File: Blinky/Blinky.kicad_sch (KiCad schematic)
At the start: 69 parts, among them J1 Conn_01x06_Socket, J2 Conn_01x06_Socket, J3 Battery Connector, J4 Charging Notches, Q1 IRLML6244, Q2 IRLML6244, Q3 IRLML6244, Q4 IRLML6244, Q5 IRLML6244, Q6 IRLML6244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

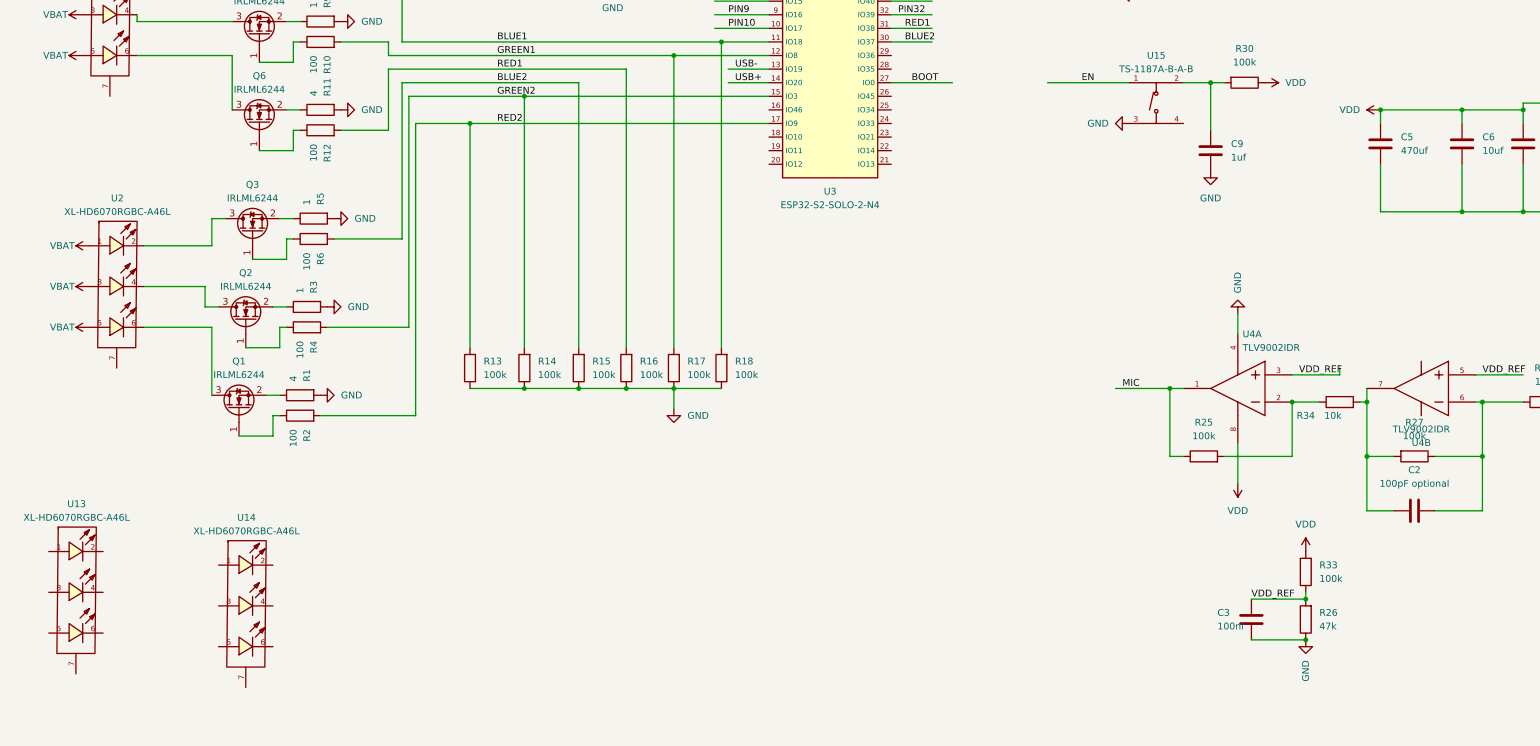
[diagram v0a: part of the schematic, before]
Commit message: reordered and fixed stuff
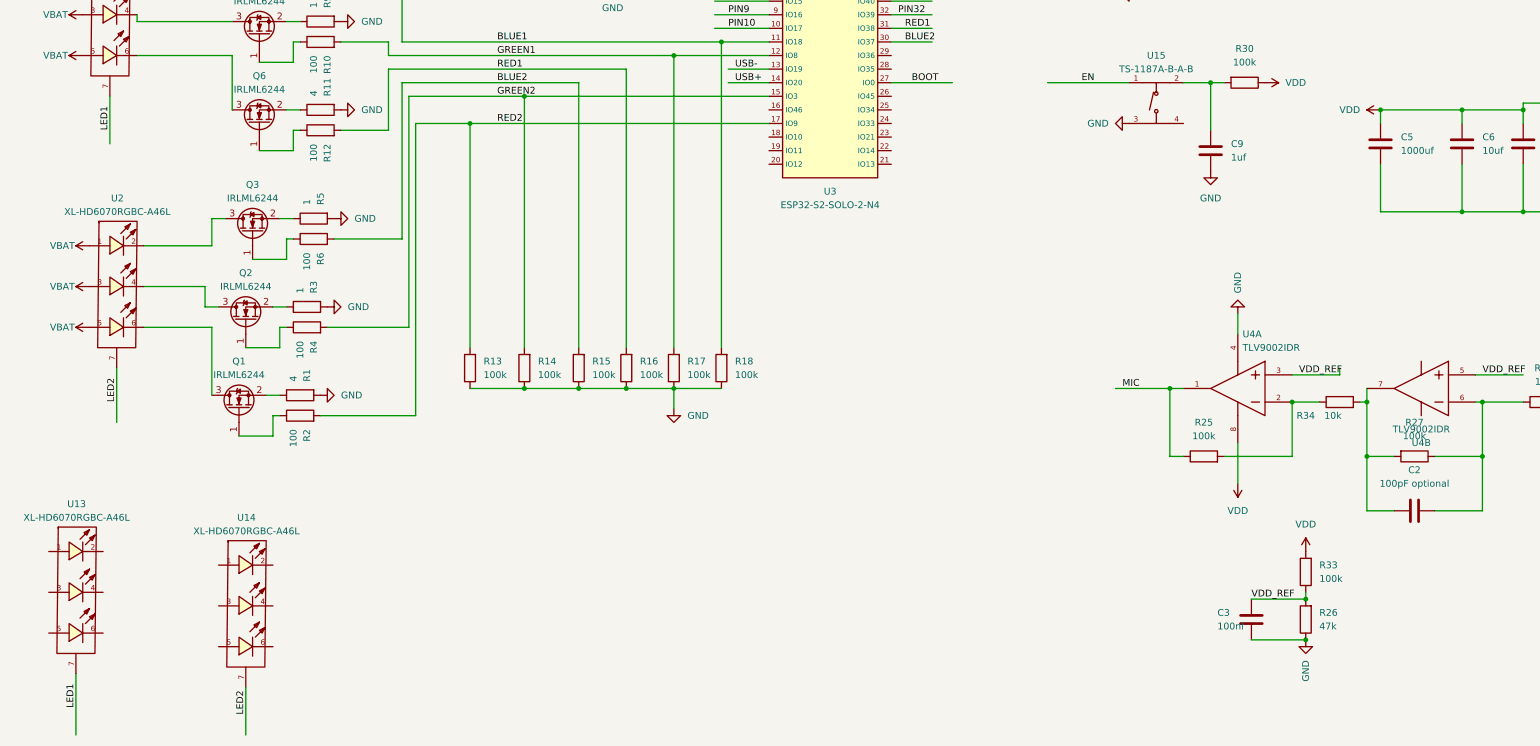
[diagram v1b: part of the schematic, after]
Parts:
- C5: value 470uf -> 1000uf; footprint Capacitor_SMD:C_0603_1608Metric -> footprint6:CAP-SMD_BD8.0-L8.3-W8.3-FD
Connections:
- net LED1: now reaches U1.7
- net LED1: now also U13.7
- net LED2: now reaches U2.7
- net LED2: now also U14.7
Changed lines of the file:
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@@
+    (stroke (width 0) (type default))
+  )
+  (wire (pts (xy 67.31 198.12) (xy 67.31 208.28))
     (stroke (width 0) (type default))
   )
@@
     (stroke (width 0) (type default))
   )
+  (wire (pts (xy 59.69 255.27) (xy 59.69 266.7))
+    (stroke (width 0) (type default))
+  )
   (wire (pts (xy 313.69 214.63) (xy 322.58 214.63))
     (stroke (width 0) (type default))
@@
     (stroke (width 0) (type default))
   )
+  (wire (pts (xy 91.44 257.81) (xy 91.44 266.7))
+    (stroke (width 0) (type default))
+  )
   (wire (pts (xy 318.77 99.06) (xy 318.77 106.68))
     (stroke (width 0) (type default))
@@
     (stroke (width 0) (type default))
   )
+  (wire (pts (xy 66.04 147.32) (xy 66.04 156.21))
+    (stroke (width 0) (type default))
+  )
   (wire (pts (xy 318.77 93.98) (xy 318.77 99.06))
     (stroke (width 0) (type default))
@@
     (effects (font (size 1.27 1.27)) (justify left bottom))
   )
+  (label "LED1" (at 66.04 153.67 90) (fields_autoplaced)
+    (effects (font (size 1.27 1.27)) (justify left bottom))
+  )
   (label "PIN6" (at 247.65 95.25 0) (fields_autoplaced)
     (effects (font (size 1.27 1.27)) (justify left bottom))
@@
     (effects (font (size 1.27 1.27)) (justify left bottom))
   )
+  (label "LED2" (at 67.31 204.47 90) (fields_autoplaced)
+    (effects (font (size 1.27 1.27)) (justify left bottom))
+  )
   (label "BAT+" (at 365.76 38.1 0) (fields_autoplaced)
     (effects (font (size 1.27 1.27)) (justify left bottom))
@@
     (effects (font (size 1.27 1.27)) (justify left bottom))
   )
+  (label "LED1" (at 59.69 261.62 90) (fields_autoplaced)
+    (effects (font (size 1.27 1.27)) (justify left bottom))
+  )
   (label "PIN6" (at 181.61 124.46 0) (fields_autoplaced)
     (effects (font (size 1.27 1.27)) (justify left bottom))
@@
   )
   (label "BAT-" (at 365.76 40.64 0) (fields_autoplaced)
+    (effects (font (size 1.27 1.27)) (justify left bottom))
+  )
+  (label "LED2" (at 91.44 262.89 90) (fields_autoplaced)
     (effects (font (size 1.27 1.27)) (justify left bottom))
   )
@@
       (effects (font (size 1.27 1.27)) (justify left))
     )
-    (property "Value" "470uf" (at 307.34 157.48 0)
+    (property "Value" "1000uf" (at 307.34 157.48 0)
       (effects (font (size 1.27 1.27)) (justify left))
     )
-    (property "Footprint" "Capacitor_SMD:C_0603_1608Metric" (at 304.4952 160.02 0)
-      (effects (font (size 1.27 1.27)) hide)
-    )
+    (property "Footprint" "footprint6:CAP-SMD_BD8.0-L8.3-W8.3-FD" (at 304.4952 160.02 0)
+      (effects (font (size 1.27 1.27)) hide)
+    )

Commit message: review by blueloop
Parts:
- removed U13, U14: XL-HD6070RGBC-A46L, footprint:LED-SMD_XL-HD6070RGBC-A46L-BACKSIDE, symbol XL-HD6070RGBC-A46L:XL-HD6070RGBC-A46L
- added C12: 100nF, Capacitor_SMD:C_0603_1608Metric, symbol Device:C
- added R19, R24: 470k, Resistor_SMD:R_0603_1608Metric, symbol Device:R
- LED1: renamed from U1; footprint footprint:LED-SMD_XL-HD6070RGBC-A46L -> Library:LED-SMD_XL-HD6070RGBC-A46L
- LED2: renamed from U2; footprint footprint:LED-SMD_XL-HD6070RGBC-A46L -> Library:LED-SMD_XL-HD6070RGBC-A46L
- renumbered U7 to MIC1, U12 to SW1, U11 to T1, U15 to T2
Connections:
- net GND: now also C12.1, R24.2
- net VBAT: now also R19.1
- net VBAT_MESS: now reaches U3.4 (IO4)
- net VBAT_MESS: now also C12.2, R19.2, R24.1

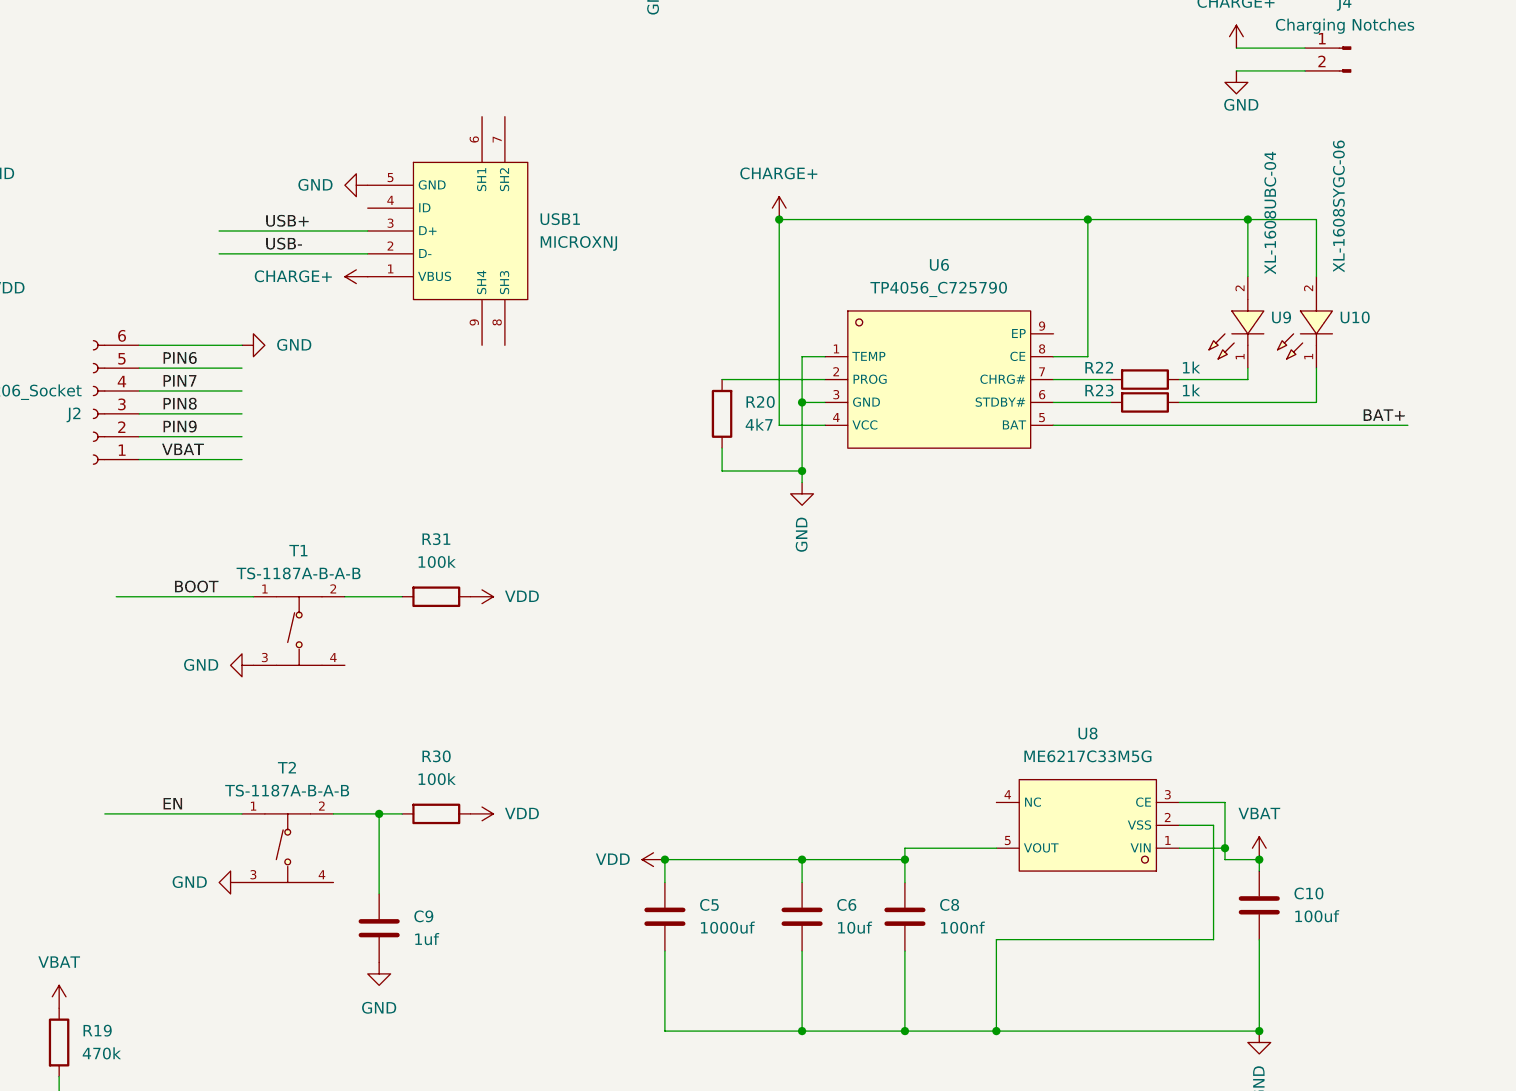
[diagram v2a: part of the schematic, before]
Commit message: 3d work and fixed 90 deg rotation in capacitor issue
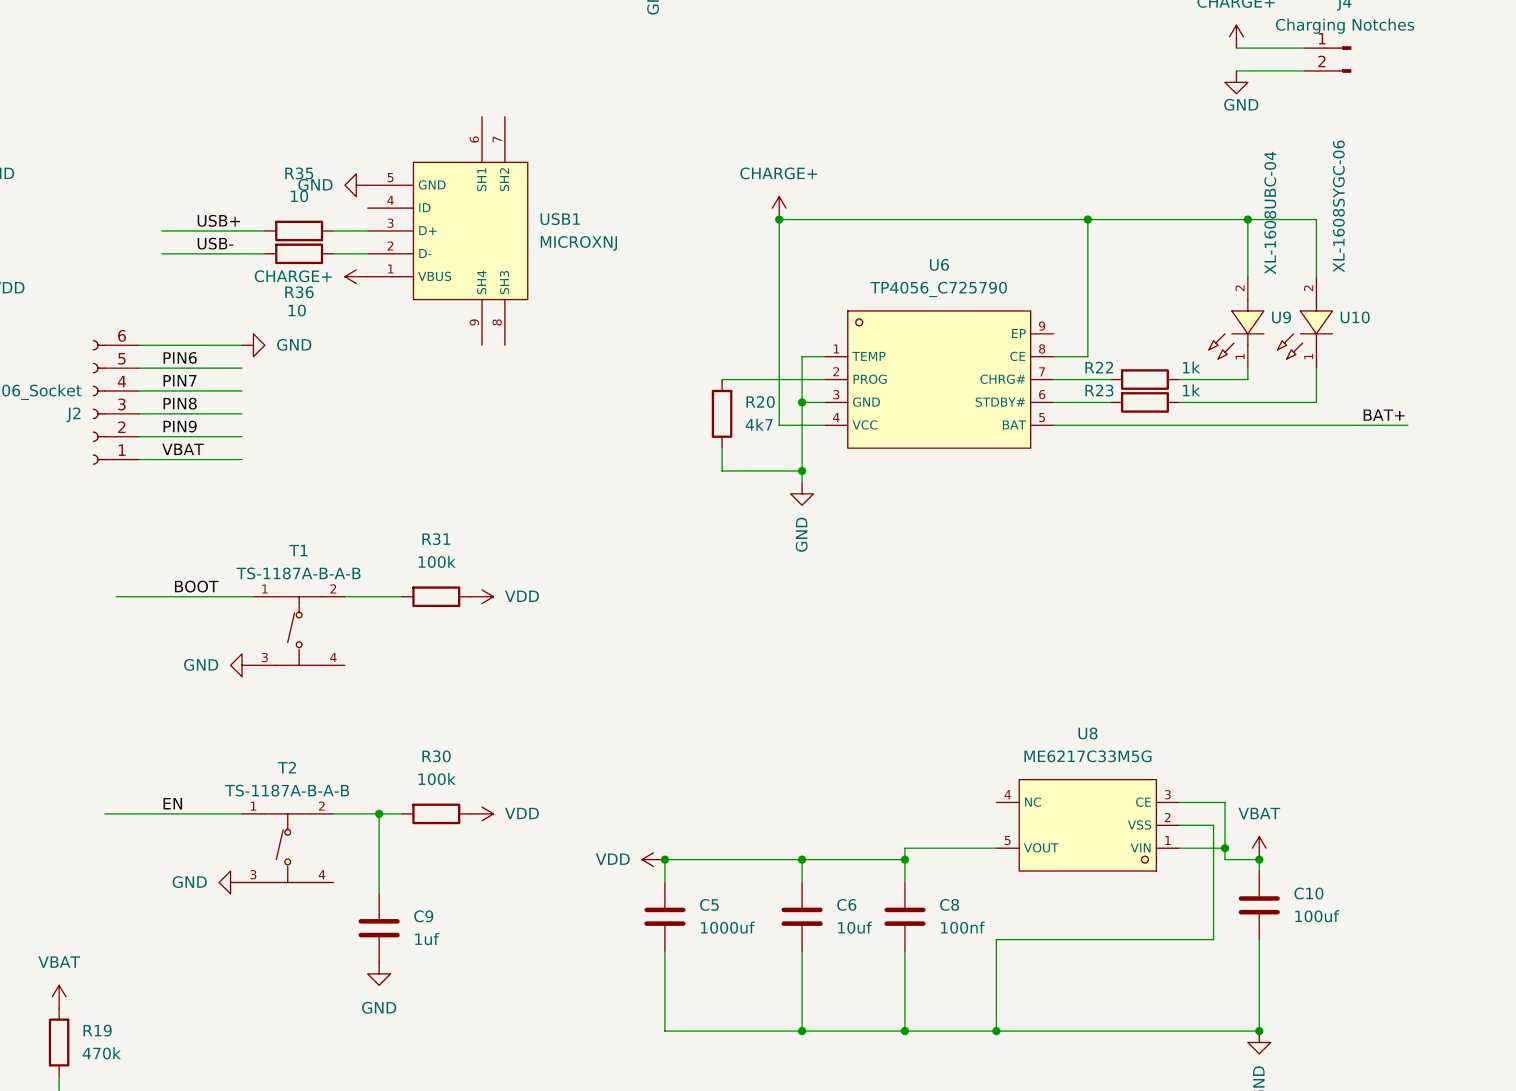
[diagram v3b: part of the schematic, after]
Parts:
- added R35, R36: 10, Resistor_SMD:R_0603_1608Metric, symbol Device:R
- C10: footprint Capacitor_SMD:C_0603_1608Metric -> footprint:CASE-B_3528
- J1, J2: footprint Connector_PinSocket_2.54mm:PinSocket_1x06_P2.54mm_Vertical -> footprint:HDR-TH_6P-P2.54-V-F
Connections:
- net GND: now also C10.2; no longer C10.1
- net USB+: now also R35.2; no longer USB1.3 (D+)
- net USB-: now also R36.2; no longer USB1.2 (D-)
- net VBAT: now also C10.1; no longer C10.2
- new net: R36.1, USB1.2 (D-)
- new net: R35.1, USB1.3 (D+)
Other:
- moved on the sheet: C10
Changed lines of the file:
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@@
 	(wire
 		(pts
-			(xy 254 80.01) (xy 270.51 80.01)
+			(xy 247.65 80.01) (xy 259.08 80.01)
 		)
 		(stroke
@@
 	(wire
 		(pts
-			(xy 254 82.55) (xy 270.51 82.55)
+			(xy 247.65 82.55) (xy 259.08 82.55)
 		)
 		(stroke
@@
 	(wire
 		(pts
+			(xy 266.7 80.01) (xy 270.51 80.01)
+		)
+		(stroke
+			(width 0)
+			(type default)
+		)
+	)
+	(wire
+		(pts
 			(xy 264.16 201.93) (xy 264.16 214.63)
 		)
@@
 	(wire
 		(pts
+			(xy 266.7 82.55) (xy 270.51 82.55)
+		)
+		(stroke
+			(width 0)
+			(type default)
+		)
+	)
+	(wire
+		(pts
 			(xy 143.51 147.32) (xy 189.23 147.32)
 		)
@@
 	)
 	(label "USB+"
-		(at 259.08 80.01 0)
+		(at 251.46 80.01 0)
 		(fields_autoplaced yes)
 		(effects
@@
 	)
 	(label "USB-"
-		(at 259.08 82.55 0)
+		(at 251.46 82.55 0)
 		(fields_autoplaced yes)
 		(effects
@@
 	(symbol
 		(lib_id "Device:R")
+		(at 262.89 82.55 270)
+		(unit 1)
+		(exclude_from_sim no)
+		(in_bom yes)
+		(on_board yes)
+		(dnp no)
+		(property "Reference" "R36"
+			(at 262.89 86.868 90)
+			(effects
+				(font
+					(size 1.27 1.27)
+				)
+			)
+		)
+		(property "Value" "10"
+			(at 262.636 88.9 90)
+			(effects
+				(font
+					(size 1.27 1.27)
+				)
+			)
+		)
+		(property "Footprint" "Resistor_SMD:R_0603_1608Metric"
+			(at 262.89 80.772 90)
+			(effects
+				(font
+					(size 1.27 1.27)
+				)
+				(hide yes)
+			)
+		)
+		(property "Datasheet" "~"
+			(at 262.89 82.55 0)
+			(effects
+				(font
+					(size 1.27 1.27)
+				)
+				(hide yes)
+			)
+		)
+		(property "Description" "Resistor"
+			(at 262.89 82.55 0)
+			(effects
+				(font
+					(size 1.27 1.27)
+				)
+				(hide yes)
+			)
+		)
+		(pin "2"
+		)
+		(pin "1"
+		)
+		(instances
+			(project "Blinky"
+				(path "/a854b35b-60aa-44a5-a34e-fbb2d526cb93"
+					(reference "R36")
+					(unit 1)
+				)
+			)
+		)
+	)
+	(symbol
+		(lib_id "Device:R")
 		(at 101.6 207.01 90)
 		(unit 1)
@@
 	(symbol
 		(lib_id "Device:R")
+		(at 262.89 80.01 270)
+		(unit 1)
+		(exclude_from_sim no)
+		(in_bom yes)
+		(on_board yes)
+		(dnp no)
+		(fields_autoplaced yes)
+		(property "Reference" "R35"
+			(at 262.89 73.66 90)
+			(effects
+				(font
+					(size 1.27 1.27)
+				)
+			)
+		)
+		(property "Value" "10"
+			(at 262.89 76.2 90)
+			(effects
+				(font
+					(size 1.27 1.27)
+				)
+			)
+		)
+		(property "Footprint" "Resistor_SMD:R_0603_1608Metric"
+			(at 262.89 78.232 90)
+			(effects
+				(font
+					(size 1.27 1.27)
+				)
+				(hide yes)
+			)
+		)
+		(property "Datasheet" "~"
+			(at 262.89 80.01 0)
+			(effects
+				(font
+					(size 1.27 1.27)
+				)
+				(hide yes)
+			)
+		)
+		(property "Description" "Resistor"
+			(at 262.89 80.01 0)
+			(effects
+				(font
+					(size 1.27 1.27)
+				)
+				(hide yes)
+			)
+		)
+		(pin "2"
+		)
+		(pin "1"
+		)
+		(instances
+			(project "Blinky"
+				(path "/a854b35b-60aa-44a5-a34e-fbb2d526cb93"
+					(reference "R35")
+					(unit 1)
+				)
+			)
+		)
+	)
+	(symbol
+		(lib_id "Device:R")
 		(at 356.87 99.06 270)
 		(unit 1)
@@
 			)
 		)
-		(property "Footprint" "Connector_PinSocket_2.54mm:PinSocket_1x06_P2.54mm_Vertical"
+		(property "Footprint" "footprint:HDR-TH_6P-P2.54-V-F"
 			(at 213.36 81.28 0)
 			(effects
@@
 			)
 		)
-		(property "Footprint" "Connector_PinSocket_2.54mm:PinSocket_1x06_P2.54mm_Vertical"
+		(property "Footprint" "footprint:HDR-TH_6P-P2.54-V-F"
 			(at 240.03 100.33 0)
 			(effects
@@
 	(symbol
 		(lib_id "Device:C")
-		(at 369.57 154.94 180)
+		(at 369.57 154.94 0)
 		(unit 1)
 		(exclude_from_sim no)
@@
 		(fields_autoplaced yes)
 		(property "Reference" "C10"
-			(at 373.38 153.67 0)
+			(at 373.38 153.6699 0)
 			(effects
 				(font
 					(size 1.27 1.27)
 				)
-				(justify right)
+				(justify left)
 			)
 		)
 		(property "Value" "100uf"
-			(at 373.38 156.21 0)
+			(at 373.38 156.2099 0)
 			(effects
 				(font
 					(size 1.27 1.27)
 				)
-				(justify right)
+				(justify left)
 			)
 		)
-		(property "Footprint" "Capacitor_SMD:C_0603_1608Metric"
-			(at 368.6048 151.13 0)
+		(property "Footprint" "footprint:CASE-B_3528"
+			(at 370.5352 158.75 0)
 			(effects
 				(font

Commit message: zwischenstand
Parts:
- added C13, C14: 18pf, Capacitor_SMD:C_0603_1608Metric, symbol Device:C
- added TXAL1: Q13FC1350000400, footprint3:FC-135R_L3.2-W1.5, symbol Q13FC1350000400:Q13FC1350000400
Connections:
- net PIN10 is gone; now on net BLUE1: U3.10 (IO17)
- net BLUE1: no longer U3.11 (IO18)
- net GND: now also C13.2, C14.2
- net PIN36: now reaches U3.36 (RXD0)
- net PIN36: now also J1.3 (Pin_3)
- net PIN37: now reaches U3.37 (TXD0)
- net PIN37: now also J1.2 (Pin_2)
- net PIN32 renamed 32_32khz
- net 32_32khz: now also C14.1, TXAL1.2; no longer J1.2 (Pin_2)
- net PIN33 renamed 33_32khz
- net 33_32khz: now also C13.1, TXAL1.1; no longer J1.3 (Pin_3)

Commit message: board v3 0.8
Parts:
- added J5: Battery Connector, Connector_JST:JST_PH_B2B-PH-K_1x02_P2.00mm_Vertical, symbol Connector_Generic:Conn_01x02
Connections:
- net BAT+: now also J5.1 (Pin_1)
- net BAT-: now also J5.2 (Pin_2)
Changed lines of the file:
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@@
 	(wire
 		(pts
+			(xy 367.03 30.48) (xy 372.11 30.48)
+		)
+		(stroke
+			(width 0)
+			(type default)
+		)
+	)
+	(wire
+		(pts
 			(xy 368.3 95.25) (xy 368.3 96.52)
 		)
@@
 	(wire
 		(pts
+			(xy 367.03 33.02) (xy 372.11 33.02)
+		)
+		(stroke
+			(width 0)
+			(type default)
+		)
+	)
+	(wire
+		(pts
 			(xy 201.93 234.95) (xy 201.93 237.49)
 		)
@@
 		)
 	)
+	(label "BAT-"
+		(at 368.3 33.02 0)
+		(fields_autoplaced yes)
+		(effects
+			(font
+				(size 1.27 1.27)
+			)
+			(justify left bottom)
+		)
+	)
 	(label "GREEN2"
 		(at 138.43 147.32 0)
@@
 		)
 	)
+	(label "BAT+"
+		(at 368.3 30.48 0)
+		(fields_autoplaced yes)
+		(effects
+			(font
+				(size 1.27 1.27)
+			)
+			(justify left bottom)
+		)
+	)
 	(label "PIN7"
 		(at 247.65 97.79 0)
@@
 					(unit 1)
 				)
+			)
+		)
+	)
+	(symbol
+		(lib_id "Connector_Generic:Conn_01x02")
+		(at 377.19 30.48 0)
+		(unit 1)
+		(exclude_from_sim no)
+		(in_bom yes)
+		(on_board yes)
+		(dnp no)
+		(property "Reference" "J5"
+			(at 379.73 30.48 0)
+			(effects
+				(font
+					(size 1.27 1.27)
+				)
+				(justify left)
+			)
+		)
+		(property "Value" "Battery Connector"
+			(at 379.73 33.02 0)
+			(effects
+				(font
+					(size 1.27 1.27)
+				)
+				(justify left)
+			)
+		)
+		(property "Footprint" "Connector_JST:JST_PH_B2B-PH-K_1x02_P2.00mm_Vertical"
+			(at 377.19 30.48 0)
+			(effects
+				(font
+					(size 1.27 1.27)
+				)
+				(hide yes)
+			)
+		)
+		(property "Datasheet" "~"
+			(at 377.19 30.48 0)
+			(effects
+				(font
+					(size 1.27 1.27)
+				)
+				(hide yes)
+			)
+		)
+		(property "Description" ""
+			(at 377.19 30.48 0)
+			(effects
+				(font
+					(size 1.27 1.27)
+				)
+				(hide yes)
+			)
+		)
+		(pin "1"
+		)
+		(pin "2"
+		)
+		(instances
+			(project "Blinky"
+				(path "/a854b35b-60aa-44a5-a34e-fbb2d526cb93"
+					(reference "J5")
+					(unit 1)
+				)
